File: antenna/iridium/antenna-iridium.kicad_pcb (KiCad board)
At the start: 4 copper layers, 60 x 60 mm, 37 parts, among them J1 GSG-USB-MICRO-B-SHIELDED, P1 ANT, P2 CONN_COAX, U1 MGA-61563, U2 EPCOS_DCC6C, U3 ADP151_TSOT, U4 MGA-61563

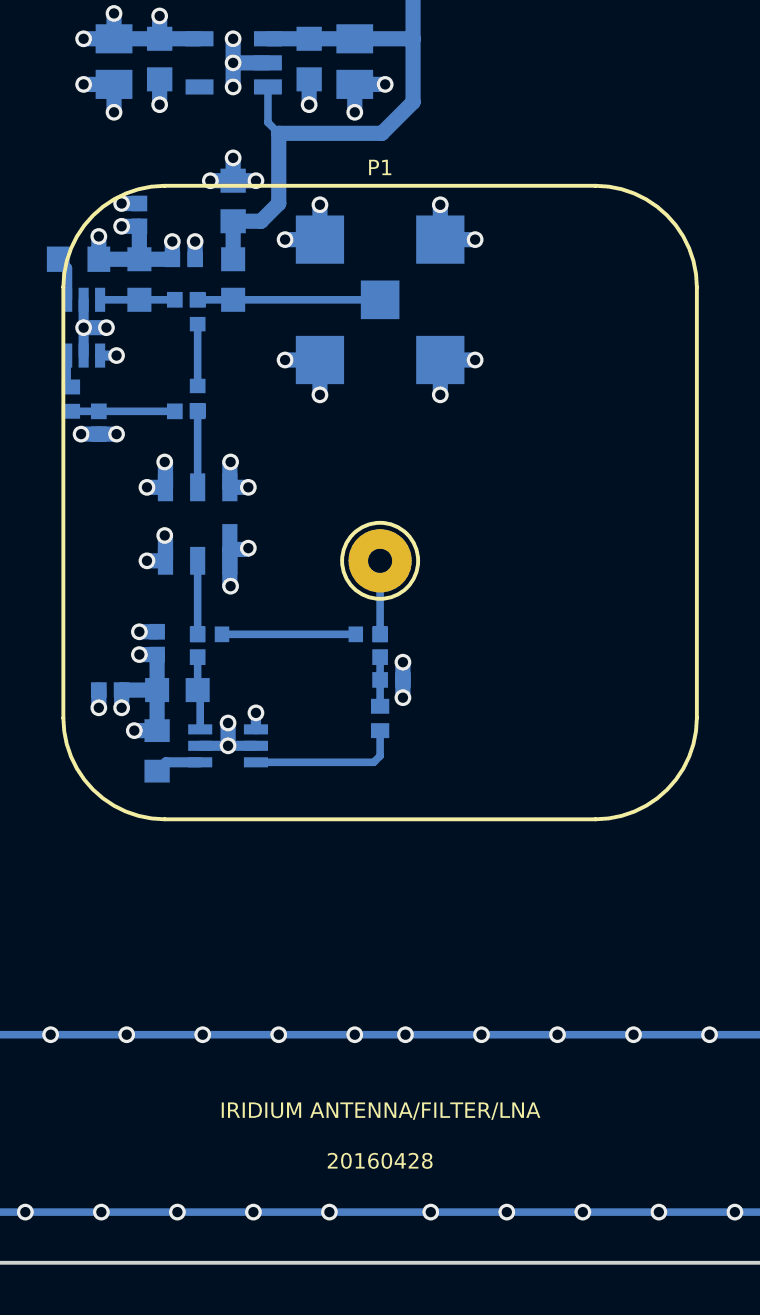
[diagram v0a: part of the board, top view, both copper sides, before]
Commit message: Iridium antenna: Silk/mask clean-up, company name, make Gerbers.
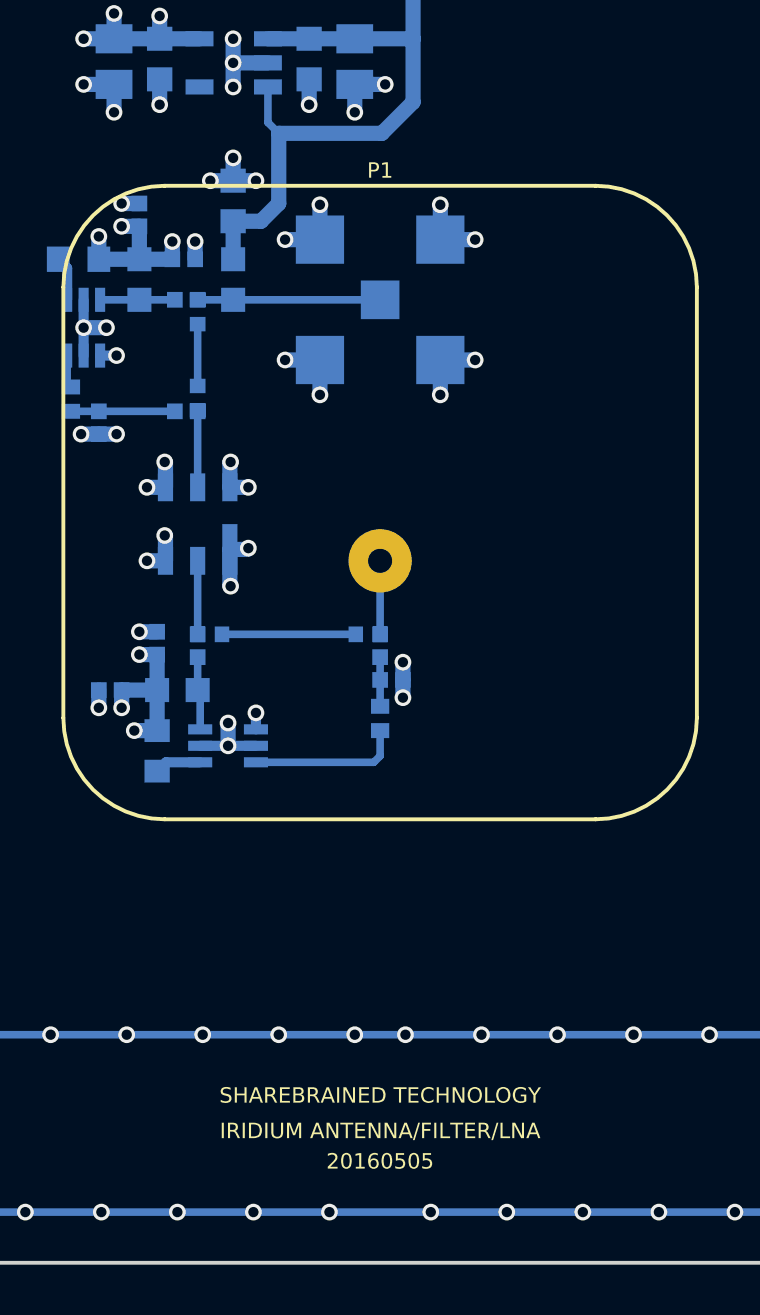
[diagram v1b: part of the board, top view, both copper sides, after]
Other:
- rule pad_to_mask_clearance: 0.2 -> 0.0762
- board text added: "20160505"
- board text added: "SHAREBRAINED TECHNOLOGY"
- board text removed: "20160428"
